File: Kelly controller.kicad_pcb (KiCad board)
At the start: 2 copper layers, 106.5 x 97.2 mm, 32 parts, among them J1 Conn_01x06_Female, J10 48V, J11 Conn_01x06_Female, J12 Conn_01x06_Female, J2 Conn_01x06_Female, J3 I2C throttle, J5 48V, J6 12V, J7 5V, J8 12V, J9 5V, SW1 FNR, SW2 Brake_SW, SW4 Power Switch, SW5 Power Switch, U1 LTV-247, U2 LTV-247, U3 MCP4251-xxxx-P

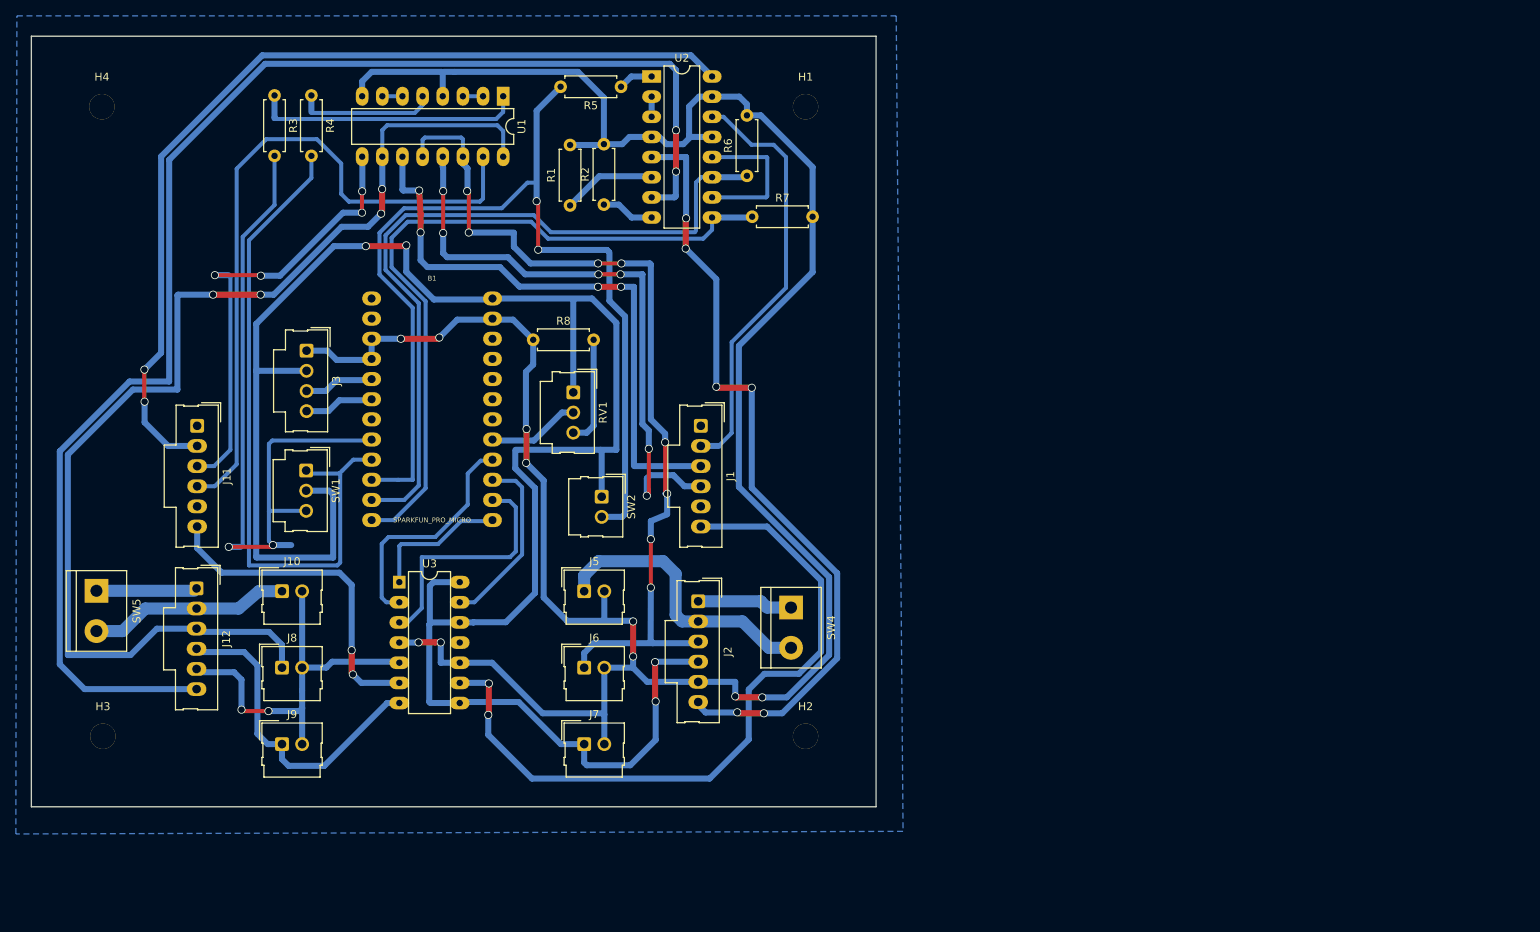
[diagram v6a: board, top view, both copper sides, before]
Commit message: Last version of mcp4251 based board. Too many problems but ultimately got to work by combining grounds and putting diodes in line with pot high side to get lower that Arduino Vcc. Next version will use PWM buffered by opamp
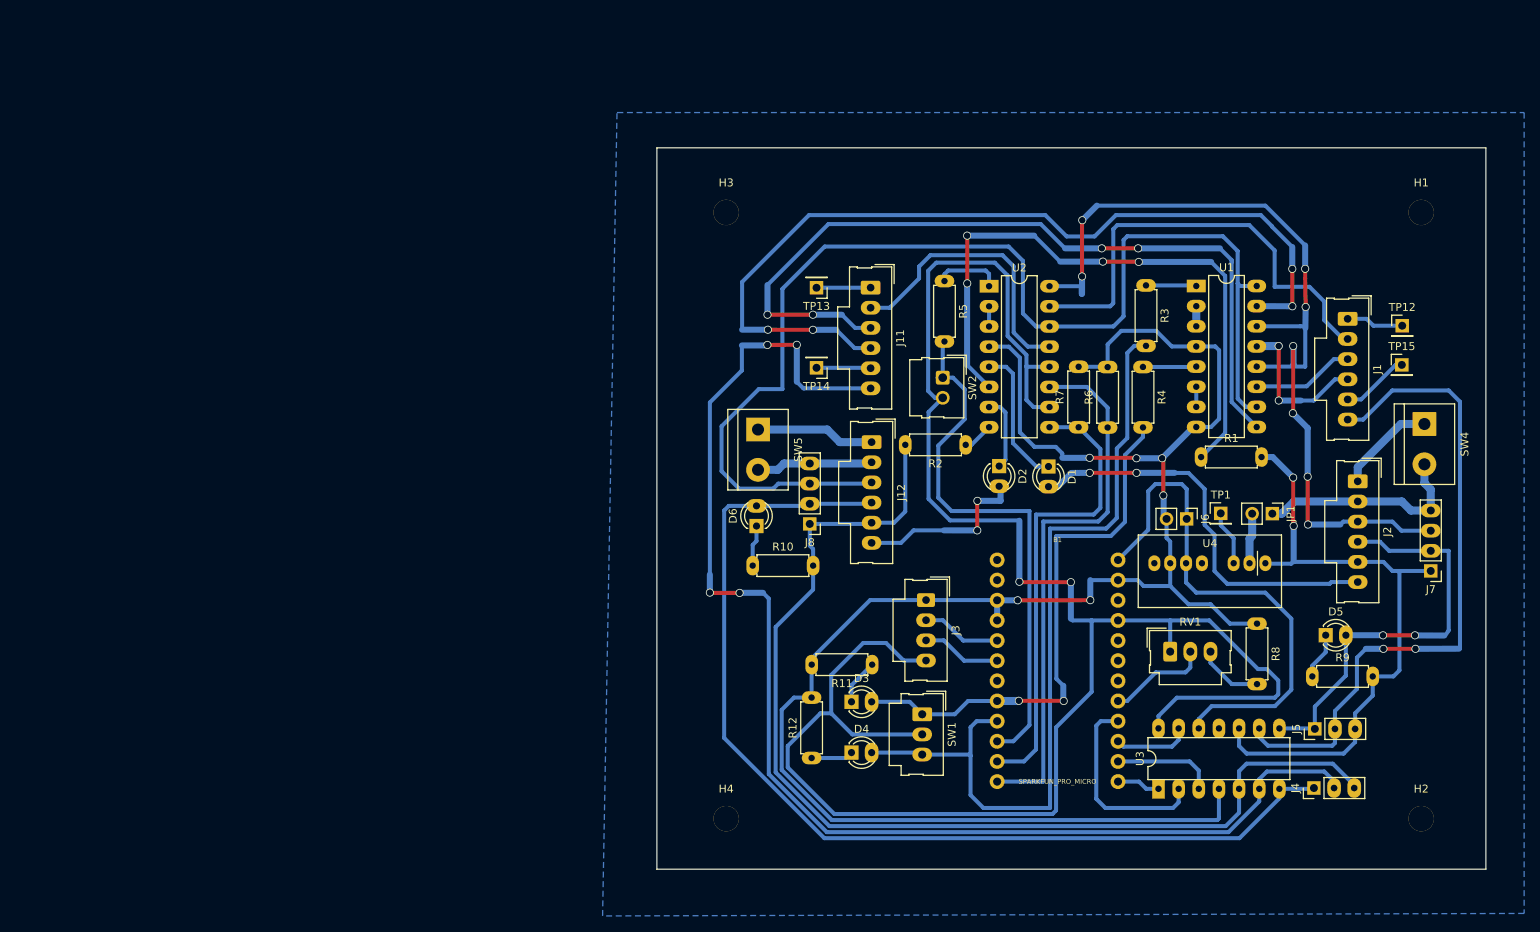
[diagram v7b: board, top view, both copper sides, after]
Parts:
- removed J10: 48V, Connector_Molex:Molex_SL_171971-0002_1x02_P2.54mm_Vertical
- removed J9: 5V, Connector_Molex:Molex_SL_171971-0002_1x02_P2.54mm_Vertical
- added D1: yellow, myfootprints:LED_D3.0mm_wide_pads, F.Cu at (142.2, 86.6)
- added D2: yellow, myfootprints:LED_D3.0mm_wide_pads, F.Cu at (136.0, 86.6)
- added D3: green, myfootprints:LED_D3.0mm_wide_pads, F.Cu at (117.4, 116.3)
- added D4: green, myfootprints:LED_D3.0mm_wide_pads, F.Cu at (117.4, 122.7)
- added D5: RED, myfootprints:LED_D3.0mm_wide_pads, F.Cu at (177.2, 107.9)
- added D6: RED, myfootprints:LED_D3.0mm_wide_pads, F.Cu at (105.4, 94.1)
- added J4: throttle A, myfootprints:PinHeader_1x03_P2.54mm_Vertical_wide_pads, F.Cu at (175.7, 127.2)
- added JP1: Jumper, Connector_PinHeader_2.54mm:PinHeader_1x02_P2.54mm_Vertical, F.Cu at (170.5, 92.6)
- added R10: 1k, myfootprints:R_Axial_DIN0207_L6.3mm_D2.5mm_P7.62mm_Horizontal_wide_pads, F.Cu at (104.9, 99.1)
- added R11: 1k, myfootprints:R_Axial_DIN0207_L6.3mm_D2.5mm_P7.62mm_Horizontal_wide_pads, F.Cu at (120.0, 111.6)
- added R12: 1k, myfootprints:R_Axial_DIN0207_L6.3mm_D2.5mm_P7.62mm_Horizontal_wide_pads, F.Cu at (112.4, 123.4)
- added R9: 1k, myfootprints:R_Axial_DIN0207_L6.3mm_D2.5mm_P7.62mm_Horizontal_wide_pads, F.Cu at (175.5, 113.1)
- added TP1: RC, Connector_PinHeader_2.54mm:PinHeader_1x01_P2.54mm_Vertical, F.Cu at (164.0, 92.5)
- added TP12: ftsw, Connector_PinHeader_2.54mm:PinHeader_1x01_P2.54mm_Vertical, F.Cu at (186.8, 68.9)
- added TP13: ftsw, Connector_PinHeader_2.54mm:PinHeader_1x01_P2.54mm_Vertical, F.Cu at (113.0, 64.1)
- added TP14: anbrk, Connector_PinHeader_2.54mm:PinHeader_1x01_P2.54mm_Vertical, F.Cu at (113.0, 74.2)
- added TP15: anbrk, Connector_PinHeader_2.54mm:PinHeader_1x01_P2.54mm_Vertical, F.Cu at (186.8, 73.8)
- added U4: SPAN02C-05, myfootprints:SPAN02, F.Cu at (162.6, 98.8)
- J1, J11, J12, J2: footprint Connector_Molex:Molex_SL_171971-0006_1x06_P2.54mm_Vertical -> myfootprints:Molex_SL_171971-0006_1x06_P2.54mm_Vertical
- J3: footprint Connector_Molex:Molex_SL_171971-0004_1x04_P2.54mm_Vertical -> myfootprints:Molex_SL_171971-0004_1x04_P2.54mm_Vertical_wide_pads
- J5: value 48V -> throttle B; footprint Connector_Molex:Molex_SL_171971-0002_1x02_P2.54mm_Vertical -> myfootprints:PinHeader_1x03_P2.54mm_Vertical_wide_pads
- J6: value 12V -> Board power; footprint Connector_Molex:Molex_SL_171971-0002_1x02_P2.54mm_Vertical -> Connector_PinHeader_2.54mm:PinHeader_1x02_P2.54mm_Vertical
- J7: value 5V -> B_5_12_48; footprint Connector_Molex:Molex_SL_171971-0002_1x02_P2.54mm_Vertical -> myfootprints:PinHeader_1x04_P2.54mm_Vertical_wide_pads
- J8: value 12V -> A_5_12_48; footprint Connector_Molex:Molex_SL_171971-0002_1x02_P2.54mm_Vertical -> myfootprints:PinHeader_1x04_P2.54mm_Vertical_wide_pads
- R1, R2, R3, R4, R5, R6, R7, R8: footprint Resistor_THT:R_Axial_DIN0207_L6.3mm_D2.5mm_P7.62mm_Horizontal -> myfootprints:R_Axial_DIN0207_L6.3mm_D2.5mm_P7.62mm_Horizontal_wide_pads
- RV1, SW1: footprint Connector_Molex:Molex_SL_171971-0003_1x03_P2.54mm_Vertical -> myfootprints:Molex_SL_171971-0003_1x03_P2.54mm_Vertical_wide_pads
- U3: value MCP4251-xxxx-P -> MCP4251
- moved H4 119.4 mm to (101.6, 131.0)
- moved R3 112.5 mm to (154.5, 63.8)
- moved R4 110.3 mm to (154.2, 74.1)
- moved J7 109.0 mm to (190.4, 99.8), turned to 180 degrees
- moved H3 102.7 mm to (101.6, 54.6)
- moved U3 99.2 mm to (156.1, 127.3), turned to 90 degrees
- moved R8 98.0 mm to (168.5, 106.5), turned to 270 degrees
- moved J5 93.7 mm to (175.8, 119.7), turned to 90 degrees
- moved U1 90.6 mm to (160.9, 63.9), turned to 0 degrees
- moved J12 87.1 mm to (119.9, 83.6)
- moved J11 86.7 mm to (119.8, 64.1)
- moved SW5 85.9 mm to (105.6, 82.0)
- moved R1 85.7 mm to (161.5, 85.4), turned to 0 degrees
- moved B1 85.5 mm to (143.4, 111.1)
- moved J2 84.5 mm to (181.2, 88.5)
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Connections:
- net /FWD renamed /FWD-B
- net /PWR renamed /PWR-B
- net /REV renamed /REV-B
- B1 pad 11: /8-Meter -> /8-Meter_A
- B1 pad 12: /9-Meter -> /9-Meter_B
- B1 pad 21: Net-(B1-Pad21) -> VCC
- B1 pad 8: /5-Forward -> /5-Reverse
- B1 pad 9: /6-Reverse -> /6-Forward
- J1 pad 1: /Foot_SW -> /Foot_SW-B
- J1 pad 2: /Brake -> /Brake-B
- J1 pad 5: /Brake_AN -> /Brake_AN-B
- J1 pad 6: /Throttle -> /Throttle-B
- J2 pad 2: +48V -> +48VB
- J2 pad 3: 12V -> +12VB
- J2 pad 4: 5V -> +5VB
- J2 pad 5: GND -> GNDB
- J2 pad 6: /Meter -> /Meter-B
- J3 pad 2: 5V -> /SDA
- J3 pad 3: /SDA -> /SCL
- J3 pad 4: /SCL -> VCC
- J5 pad 1: +48V -> +5VB
- J5 pad 2: GND -> /Throttle-B
- J6 pad 1: 12V -> 5V
- J7 pad 1: 5V -> GNDB
- J7 pad 2: GND -> +5VB
- J8 pad 1: +12VA -> GNDA
- J8 pad 2: GNDA -> +5VA
- R1 pad 2: GND -> GNDB
- R2 pad 2: GND -> GNDA
- R3 pad 2: /5-Forward -> /6-Forward
- R4 pad 2: /6-Reverse -> /5-Reverse
- R6 pad 1: /8-Meter -> /9-Meter_B
- R7 pad 1: /9-Meter -> /8-Meter_A
- RV1 pad 1: 5V -> VCC
- SW1 pad 1: /6-Reverse -> /5-Reverse
- SW1 pad 2: 5V -> VCC
- SW1 pad 3: /5-Forward -> /6-Forward
- SW2 pad 1: 5V -> /7-Brake
- SW2 pad 2: /7-Brake -> VCC
- SW4 pad 2: +48V -> +48VB
- U1 pad 12: 12V -> +12VB
- U1 pad 14: 12V -> +12VB
- U2 pad 10: /VCC -> VCC
- U2 pad 11: /8-Meter -> /9-Meter_B
- U2 pad 12: /VCC -> VCC
- U2 pad 13: GND -> /Brake-A
- U2 pad 14: /Brake -> +12VA
- U2 pad 15: GND -> /Brake-B
- U2 pad 16: /Brake-A -> +12VB
- U2 pad 5: /Meter -> Net-(D1-Pad1)
- U2 pad 7: /Meter-A -> Net-(D2-Pad1)
- U2 pad 9: /9-Meter -> /8-Meter_A
- U3 pad 10: GND -> GNDB
- U3 pad 14: 5V -> VCC
- U3 pad 8: 5V -> +5VB
- U3 pad 9: /Throttle -> /Throttle-B
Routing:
- net VCC: track 0.00 -> 253.2 mm, vias 0 -> 2
- net 5V: track 261.8 -> 66.0 mm, vias 4 -> 0
- net /Meter-A: track 179.0 -> 22.5 mm
- net /Throttle-A: track 41.8 -> 164.5 mm, vias 2 -> 4
- net +12VB: track 0.00 -> 114.9 mm, vias 0 -> 8
- net 12V: track 112.4 -> 0.00 mm, vias 8 -> 0
- net /6-Forward: track 0.00 -> 103.8 mm
- net /Meter: track 99.2 -> 0.00 mm, vias 6 -> 0
- net /8-Meter: track 94.0 -> 0.00 mm
- net /Throttle: track 91.7 -> 0.00 mm, vias 2 -> 0
- net /5-Forward: track 91.2 -> 0.00 mm, vias 2 -> 0
- net /9-Meter: track 91.1 -> 0.00 mm
- net +5VA: track 41.1 -> 130.6 mm
- net GNDA: track 49.9 -> 138.1 mm, vias 2 -> 0
- net /6-Reverse: track 87.0 -> 0.00 mm
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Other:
- board size 106.5 x 97.2 mm -> 104.5 x 91 mm

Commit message: board ready to cut
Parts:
- removed B1: SPARKFUN_PRO_MICRO, Boards:SPARKFUN_PRO_MICRO
- removed J11, J12, J2: Conn_01x06_Female, myfootprints:Molex_SL_171971-0006_1x06_P2.54mm_Vertical
- removed R5: 220, myfootprints:R_Axial_DIN0207_L6.3mm_D2.5mm_P7.62mm_Horizontal_wide_pads
- removed R6: 10k, myfootprints:R_Axial_DIN0207_L6.3mm_D2.5mm_P7.62mm_Horizontal_wide_pads
- removed SW5: Power Switch, TerminalBlock:TerminalBlock_bornier-2_P5.08mm
- removed TP1: RC, Connector_PinHeader_2.54mm:PinHeader_1x01_P2.54mm_Vertical
- removed TP12, TP13: ftsw, Connector_PinHeader_2.54mm:PinHeader_1x01_P2.54mm_Vertical
- removed TP14, TP15: anbrk, Connector_PinHeader_2.54mm:PinHeader_1x01_P2.54mm_Vertical
- removed U2: LTV-247, Package_DIP:DIP-16_W7.62mm_LongPads
- removed U3: MCP4251, Package_DIP:DIP-14_W7.62mm
- removed U4: SPAN02C-05, myfootprints:SPAN02
- added D7: RED, myfootprints:LED_D3.0mm_wide_pads, F.Cu at (215.5, 117.3)
- added H5: STAND-OFF, Hardware:STAND-OFF, F.Cu at (224.5, 99.6)
- added H6: STAND-OFF, Hardware:STAND-OFF, F.Cu at (225.4, 130.9)
- added R13: 1k, myfootprints:R_Axial_DIN0207_L6.3mm_D2.5mm_P7.62mm_Horizontal_wide_pads, F.Cu at (216.4, 85.9)
- added R14: 1k, myfootprints:R_Axial_DIN0207_L6.3mm_D2.5mm_P7.62mm_Horizontal_wide_pads, F.Cu at (216.3, 112.0)
- added RV2: throttle(10k), Connector_PinHeader_2.54mm:PinHeader_1x06_P2.54mm_Vertical, F.Cu at (232.8, 108.8)
- added RV3: trim(1k), myfootprints:trimpot_breadboard_spacing, F.Cu at (232.7, 114.5)
- added SW3: Power Switch, TerminalBlock:TerminalBlock_bornier-2_P5.08mm, F.Cu at (216.4, 102.3)
- added TP2: T_A, Connector_PinHeader_2.54mm:PinHeader_1x01_P2.54mm_Vertical, F.Cu at (237.4, 98.6)
- added TP3: T_B, Connector_PinHeader_2.54mm:PinHeader_1x01_P2.54mm_Vertical, F.Cu at (237.4, 106.2)
- added TP4: ftsw, Connector_PinHeader_2.54mm:PinHeader_1x01_P2.54mm_Vertical, F.Cu at (206.5, 149.6)
- added TP5: ftsw, Connector_PinHeader_2.54mm:PinHeader_1x01_P2.54mm_Vertical, F.Cu at (206.1, 77.5)
- added TP6: anbrk, Connector_PinHeader_2.54mm:PinHeader_1x01_P2.54mm_Vertical, F.Cu at (206.1, 67.4)
- added TP7: anbrk, Connector_PinHeader_2.54mm:PinHeader_1x01_P2.54mm_Vertical, F.Cu at (206.4, 139.4)
- D2: value yellow -> green
- D4: value green -> yellow
- D5: value RED -> yellow
- J1: value Conn_01x06_Female -> FNR switch; footprint myfootprints:Molex_SL_171971-0006_1x06_P2.54mm_Vertical -> Connector_Molex:Molex_SL_171971-0005_1x05_P2.54mm_Vertical
- J3: value I2C throttle -> A_5_12_48; footprint myfootprints:Molex_SL_171971-0004_1x04_P2.54mm_Vertical_wide_pads -> myfootprints:PinHeader_1x04_P2.54mm_Vertical_wide_pads
- J4: value throttle A -> B_5_12_48; footprint myfootprints:PinHeader_1x03_P2.54mm_Vertical_wide_pads -> myfootprints:PinHeader_1x04_P2.54mm_Vertical_wide_pads
- J5: value throttle B -> Conn_01x06_Female; footprint myfootprints:PinHeader_1x03_P2.54mm_Vertical_wide_pads -> Connector_Molex:Molex_SL_171971-0006_1x06_P2.54mm_Vertical
- J6: value Board power -> Conn_01x06_Female; footprint Connector_PinHeader_2.54mm:PinHeader_1x02_P2.54mm_Vertical -> Connector_Molex:Molex_SL_171971-0006_1x06_P2.54mm_Vertical
- J7: value B_5_12_48 -> Conn_01x06_Female; footprint myfootprints:PinHeader_1x04_P2.54mm_Vertical_wide_pads -> Connector_Molex:Molex_SL_171971-0006_1x06_P2.54mm_Vertical
- J8: value A_5_12_48 -> Conn_01x06_Female; footprint myfootprints:PinHeader_1x04_P2.54mm_Vertical_wide_pads -> Connector_Molex:Molex_SL_171971-0006_1x06_P2.54mm_Vertical
- JP1: value Jumper -> Jumper_2_Open
- R3: value 220 -> 1k
- R4: value 220 -> 2.2k
- R7: value 10k -> 2.2k
- R8: value 1k -> 2.2k
- RV1: value Throttle -> trim(1k); footprint myfootprints:Molex_SL_171971-0003_1x03_P2.54mm_Vertical_wide_pads -> myfootprints:trimpot_breadboard_spacing
- SW1: value FNR -> Brake_SW; footprint myfootprints:Molex_SL_171971-0003_1x03_P2.54mm_Vertical_wide_pads -> Connector_Molex:Molex_SL_171971-0002_1x02_P2.54mm_Vertical
- SW2: value Brake_SW -> FNR; footprint Connector_Molex:Molex_SL_171971-0002_1x02_P2.54mm_Vertical -> myfootprints:Molex_SL_171971-0003_1x03_P2.54mm_Vertical_wide_pads
- moved D6 115.7 mm to (221.0, 89.2), turned to 270 degrees
- moved R12 110.8 mm to (222.4, 110.3), turned to 270 degrees
- moved R11 93.3 mm to (208.6, 82.6), turned to 0 degrees
- moved J8 93.2 mm to (199.1, 127.4), turned to 90 degrees
- moved R10 91.1 mm to (193.9, 119.1), turned to 180 degrees
- moved D3 87.4 mm to (189.0, 66.1)
- moved D4 83.6 mm to (191.4, 83.8)
- moved J3 83.2 mm to (208.8, 89.4), turned to 0 degrees
- moved R3 79.6 mm to (174.5, 140.8), turned to 180 degrees
- moved RV1 79.5 mm to (232.9, 84.7), turned to 180 degrees
- moved U1 72.8 mm to (179.6, 134.3)
- moved R4 65.5 mm to (174.9, 136.2), turned to 180 degrees
- moved H4 61.2 mm to (159.5, 150.7)
- moved SW4 59.2 mm to (216.3, 134.2), turned to 90 degrees
- moved H3 59.0 mm to (159.5, 66.0)
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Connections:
- D1 pad 2: /Meter-B -> /Brake-A
- D2 pad 2: /Meter-A -> /REV-A
- D3 pad 2: /5-Reverse -> /FWD-A
- D4 pad 2: /6-Forward -> /Meter-A
- D5 pad 2: +5VB -> /Meter-B
- J1 pad 1: /Foot_SW-B -> +12VA
- J1 pad 2: /Brake-B -> +12VA
- J1 pad 3: /REV-B -> /FWD-A
- J1 pad 4: /FWD-B -> /REV-A
- J1 pad 5: /Brake_AN-B -> GNDA
- J3 pad 1: GND -> GNDA
- J3 pad 2: /SDA -> +5VA
- J3 pad 3: /SCL -> +12VA
- J3 pad 4: VCC -> +48VA
- J4 pad 1: +5VA -> GNDB
- J4 pad 2: /Throttle-A -> +5VB
- J4 pad 3: GNDA -> +12VB
- J5 pad 1: +5VB -> /Foot_SW-A
- J5 pad 2: /Throttle-B -> /Brake-A
- J5 pad 3: GNDB -> /REV-A
- J6 pad 1: 5V -> /PWR-A
- J6 pad 2: GND -> +48VA
- J7 pad 1: GNDB -> /Foot_SW-B
- J7 pad 2: +5VB -> /Brake-B
- J7 pad 3: +12VB -> /REV-B
- J7 pad 4: +48VB -> /FWD-B
- J8 pad 1: GNDA -> /PWR-B
- J8 pad 2: +5VA -> +48VB
- J8 pad 3: +12VA -> +12VB
- J8 pad 4: +48VA -> +5VB
- JP1 pad 1: +48VB -> GNDA
- JP1 pad 2: Net-(JP1-Pad2) -> GNDB
- R1 pad 2: GNDB -> /REV-A
- R10 pad 1: Net-(D6-Pad1) -> GNDB
- R10 pad 2: GNDA -> Net-(D5-Pad1)
- R11 pad 1: Net-(D3-Pad1) -> GNDA
- R11 pad 2: GND -> Net-(R11-Pad2)
- R12 pad 1: Net-(D4-Pad1) -> GNDB
- R12 pad 2: GND -> Net-(R12-Pad2)
- R2 pad 2: GNDA -> /FWD-A
- R3 pad 2: /6-Forward -> /Brake-A
- R4 pad 1: Net-(R4-Pad1) -> GNDA
- R4 pad 2: /5-Reverse -> Net-(D1-Pad1)
- R7 pad 1: /8-Meter_A -> Net-(D2-Pad1)
- R7 pad 2: GND -> GNDA
- R8 pad 1: GND -> Net-(D3-Pad1)
- R8 pad 2: Net-(R8-Pad2) -> GNDA
- R9 pad 1: Net-(D5-Pad1) -> GNDA
- R9 pad 2: GNDB -> Net-(D4-Pad1)
- RV1 pad 1: VCC -> Net-(RV1-Pad1)
- RV1 pad 2: Net-(B1-Pad17) -> Net-(R11-Pad2)
- RV1 pad 3: Net-(R8-Pad2) -> (no net)
- SW1 pad 1: /5-Reverse -> /Brake-A
- SW1 pad 2: VCC -> +12VA
- SW2 pad 1: /7-Brake -> /FWD-A
- SW2 pad 2: VCC -> +12VA
- U1 pad 1: Net-(R3-Pad1) -> Net-(R2-Pad1)
- U1 pad 10: +12VA -> (no net)
- U1 pad 11: /REV-B -> /Brake-B
- U1 pad 13: /FWD-B -> /REV-B
- U1 pad 15: /FWD-A -> /FWD-B
- U1 pad 16: +12VA -> +12VB
- U1 pad 2: Net-(U1-Pad2) -> GNDA
- U1 pad 3: Net-(U1-Pad2) -> Net-(R1-Pad1)
- U1 pad 4: GND -> GNDA
- U1 pad 5: Net-(R4-Pad1) -> Net-(R3-Pad1)
- U1 pad 6: Net-(U1-Pad6) -> GNDA
- U1 pad 7: Net-(U1-Pad6) -> (no net)
- U1 pad 8: GND -> (no net)
- U1 pad 9: /REV-A -> (no net)
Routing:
- net VCC: track 253.2 -> 0.00 mm, vias 2 -> 0
- net GND: track 235.2 -> 0.00 mm, vias 6 -> 0
- net /6-Forward: track 103.8 -> 0.00 mm
- net /Throttle-A: track 164.5 -> 65.5 mm, vias 4 -> 0
- net +5VA: track 130.6 -> 38.0 mm, vias 0 -> 2
- net /Brake-A: track 35.8 -> 111.2 mm, vias 0 -> 2
- net /5-Reverse: track 69.0 -> 0.00 mm, vias 2 -> 0
- net /9-Meter_B: track 68.8 -> 0.00 mm
- net +12VB: track 114.9 -> 47.0 mm, vias 8 -> 0
- net /7-Brake: track 67.9 -> 0.00 mm
- net 5V: track 66.0 -> 0.00 mm
- net /8-Meter_A: track 58.6 -> 0.00 mm
- net Net-(R1-Pad1): track 79.0 -> 26.4 mm, vias 4 -> 0
- net GNDA: track 138.1 -> 186.8 mm
- net /Brake-B: track 57.3 -> 11.8 mm
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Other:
- board size 104.5 x 91 mm -> 89.8 x 99.6 mm
